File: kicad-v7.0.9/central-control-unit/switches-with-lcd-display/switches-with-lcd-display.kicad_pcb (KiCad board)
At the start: 2 copper layers, 115 x 85 mm, 80 parts, among them P1 112-A-S-S-20-G-38mm, P2 95293-101A03LF, P3 95293-101A03LF, P4 95293-101A03LF, P6 95293-101A03LF, Q1 PMV213SN,215, SW1 SMTS-102-2C2T, SW10 SMTS-102-2C2T, SW2 SMTS-102-2C2T, SW3 SMTS-102-2C2T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

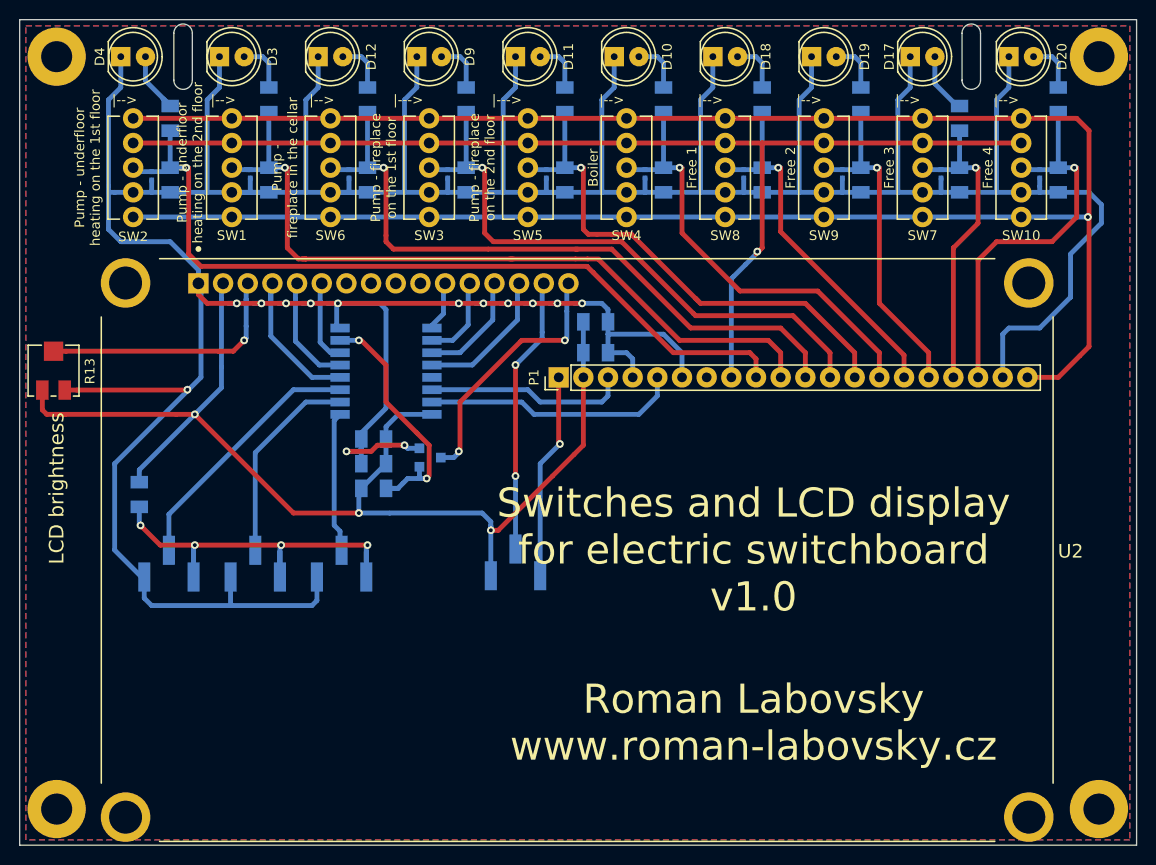
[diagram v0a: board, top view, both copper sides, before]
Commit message: Change components form library. Adding of BOM.
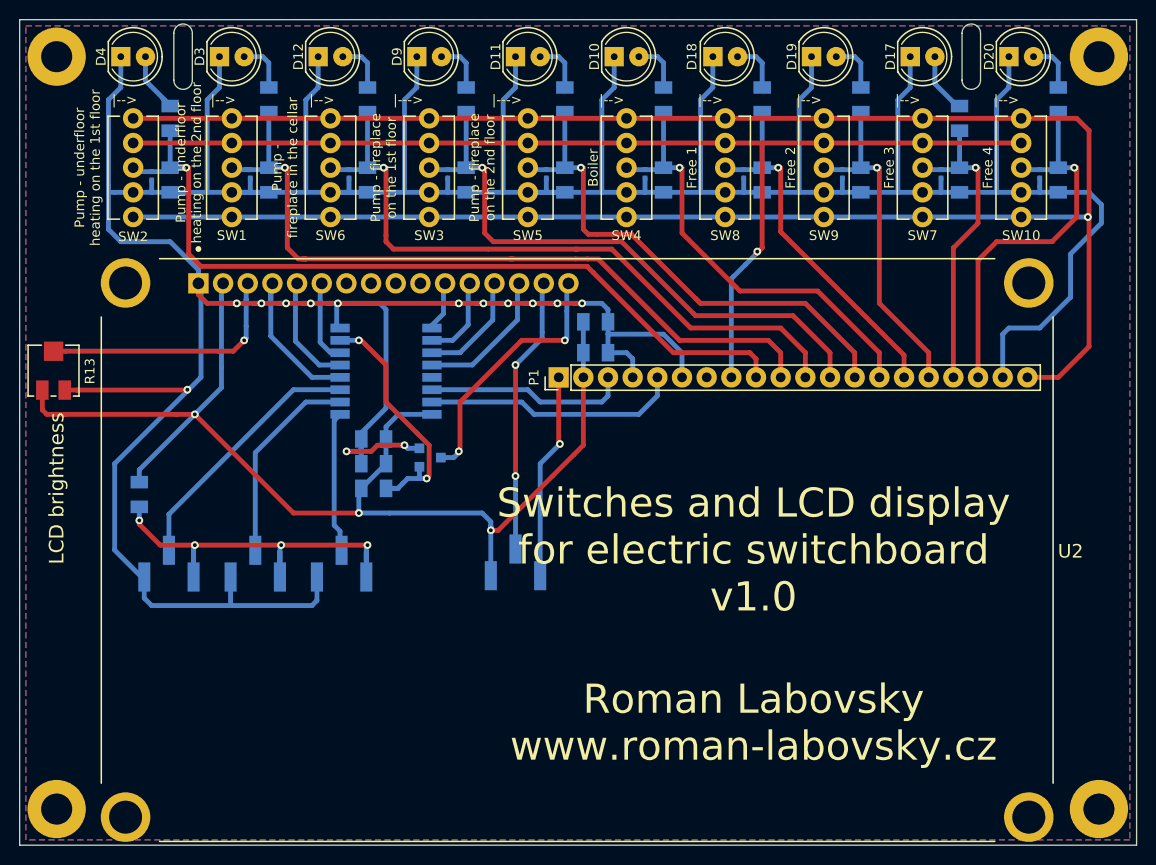
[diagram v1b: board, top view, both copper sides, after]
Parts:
- P1: footprint connector_tht_pinheader_2.54mm_rl:1x20_pinheader_2.54mm_vertical -> connector_pin_header_2.54mm_tht_rl:1x20_pin_header_2.54mm_vertical
- P2, P3, P4, P6: footprint connector_smd_pinheader_2.54mm_rl:1x3_pinheader_2.54mm_vertical -> connector_pin_header_2.54mm_smd_rl:1x3_pin_header_2.54mm_vertical
